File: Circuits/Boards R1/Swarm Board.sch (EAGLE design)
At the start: 90 parts, among them CON1 ISP(2X3), T1 NPN2N2222, T10 TEFT4300, T13 NPN2N2222, T14 NPN2N2222, T15 NPN2N2222, T16 NPN2N2222, T17 NPN2N2222, T18 NPN2N2222, T2 NPN2N2222, T3 NPN2N2222, T4 TEFT4300, T5 TEFT4300, T6 TEFT4300, T7 TEFT4300, T8 TEFT4300, T9 TEFT4300, U1 ATMEGA324P, U3 TB6552FN/FNG

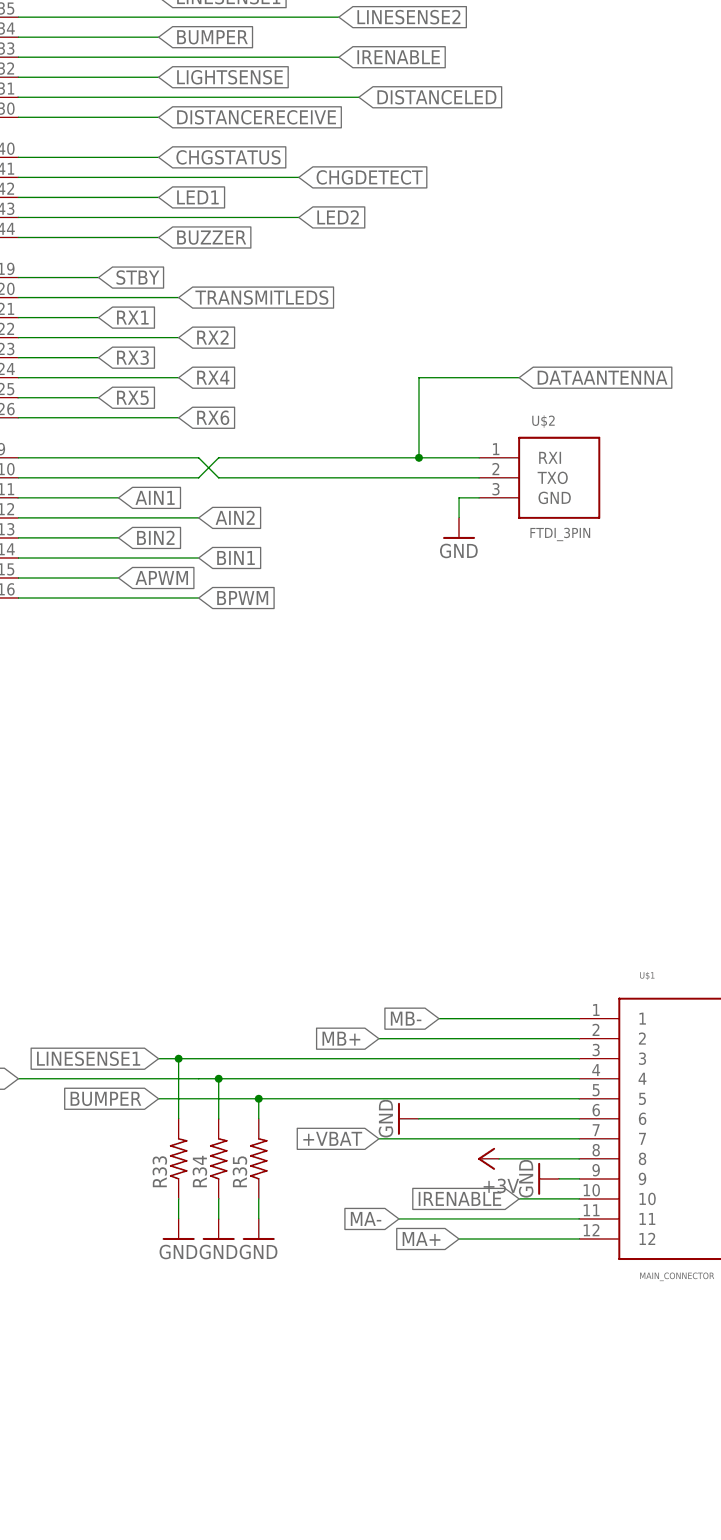
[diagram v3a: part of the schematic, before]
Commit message: 
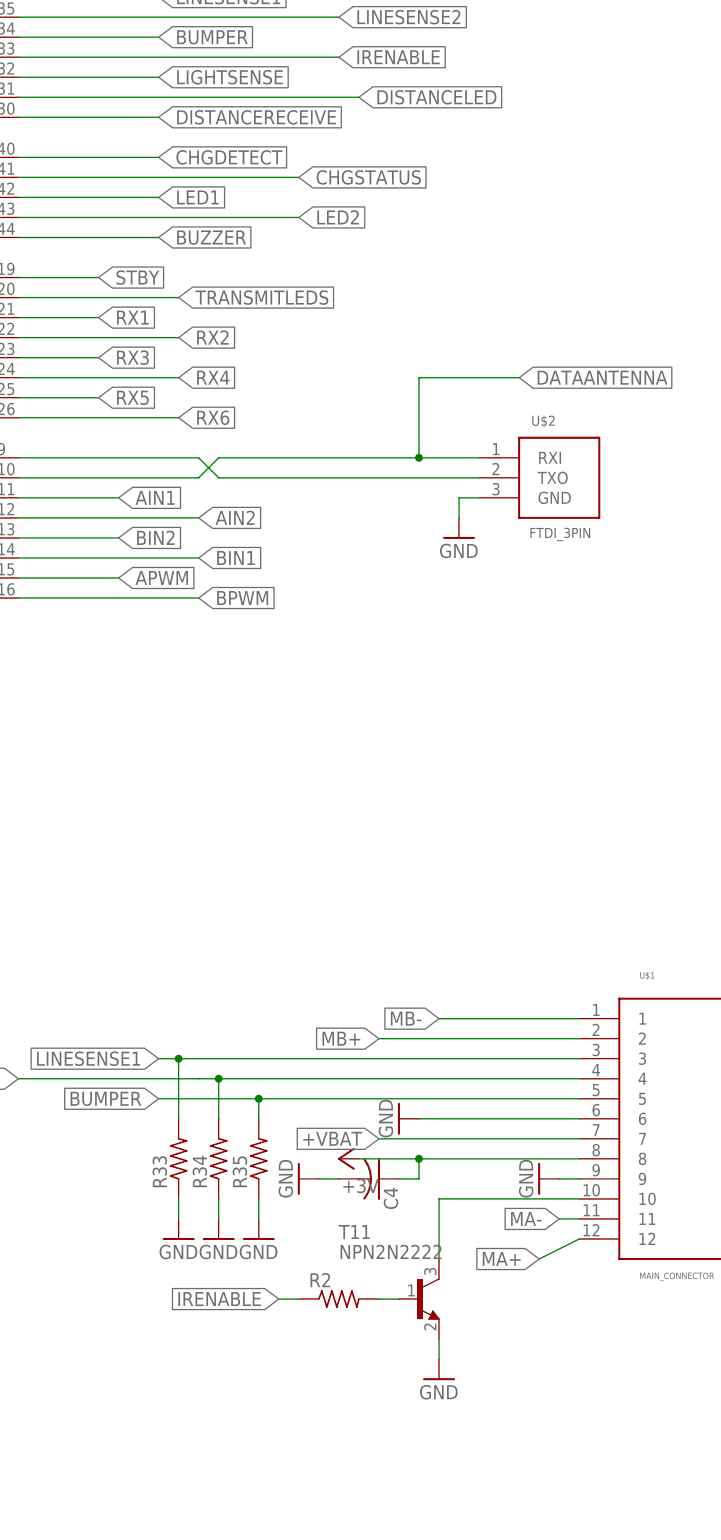
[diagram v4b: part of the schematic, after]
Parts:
- added C4: (no value), Passive:CAP0603
- added R2: (no value), Passive:RES0603
- added T11: NPN2N2222, Passive:NPN2N2222
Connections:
- new net N$4: R2.2, T11.B
- new net N$7: T11.C, U$1.10
- net +3V: now also C4.1
- net CHGDETECT: now also U1.PB0(XCK0/T0/PCINT8); no longer U1.PB1(T1/CLKO/PCINT9)
- net CHGSTATUS: now also U1.PB1(T1/CLKO/PCINT9); no longer U1.PB0(XCK0/T0/PCINT8)
- net GND: now also C4.2, T11.E
- net IRENABLE: now also R2.1; no longer U$1.10
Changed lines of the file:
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@@
 <part name="LED1" library="Passive" deviceset="LED" device="0603" value="red"/>
 <part name="R1" library="Passive" deviceset="RES" device="0603"/>
+<part name="C4" library="Passive" deviceset="CAP" device="0603"/>
+<part name="GND3" library="Supply" deviceset="GND" device=""/>
+<part name="T11" library="Passive" deviceset="NPN2N2222" device=""/>
+<part name="R2" library="Passive" deviceset="RES" device="0603"/>
+<part name="GND26" library="Supply" deviceset="GND" device=""/>
 </parts>
 <sheets>
@@
 <instance part="GND21" gate="1" x="-165.1" y="-48.26"/>
 <instance part="GND20" gate="1" x="96.52" y="-114.3" rot="R270"/>
-<instance part="P+3" gate="1" x="88.9" y="-111.76" rot="R90"/>
+<instance part="P+3" gate="1" x="71.12" y="-111.76" rot="R90"/>
 <instance part="U$3" gate="G$1" x="-114.3" y="93.98"/>
 <instance part="R29" gate="G$1" x="-66.04" y="93.98" rot="R90"/>
@@
 <instance part="LED1" gate="G$1" x="-139.7" y="114.3"/>
 <instance part="R1" gate="G$1" x="-139.7" y="101.6" rot="R90"/>
+<instance part="C4" gate="G$1" x="73.66" y="-114.3" rot="R270"/>
+<instance part="GND3" gate="1" x="66.04" y="-114.3" rot="R270"/>
+<instance part="T11" gate="G$1" x="81.28" y="-129.54"/>
+<instance part="R2" gate="G$1" x="71.12" y="-129.54"/>
+<instance part="GND26" gate="1" x="83.82" y="-139.7"/>
 </instances>
 <busses>
@@
 <segment>
 <pinref part="U$1" gate="G$1" pin="8"/>
-<wire x1="101.6" y1="-111.76" x2="91.44" y2="-111.76" width="0.1524" layer="91"/>
+<wire x1="101.6" y1="-111.76" x2="81.28" y2="-111.76" width="0.1524" layer="91"/>
 <pinref part="P+3" gate="1" pin="+3V"/>
+<pinref part="C4" gate="G$1" pin="1"/>
+<wire x1="81.28" y1="-111.76" x2="73.66" y2="-111.76" width="0.1524" layer="91"/>
+<wire x1="78.74" y1="-114.3" x2="81.28" y2="-114.3" width="0.1524" layer="91"/>
+<wire x1="81.28" y1="-114.3" x2="81.28" y2="-111.76" width="0.1524" layer="91"/>
+<junction x="81.28" y="-111.76"/>
 </segment>
 </net>
@@
 <junction x="-66.04" y="78.74"/>
 </segment>
+<segment>
+<pinref part="C4" gate="G$1" pin="2"/>
+<pinref part="GND3" gate="1" pin="GND"/>
+<wire x1="68.58" y1="-114.3" x2="71.12" y2="-114.3" width="0.1524" layer="91"/>
+</segment>
+<segment>
+<pinref part="T11" gate="G$1" pin="E"/>
+<pinref part="GND26" gate="1" pin="GND"/>
+<wire x1="83.82" y1="-137.16" x2="83.82" y2="-134.62" width="0.1524" layer="91"/>
+</segment>
 </net>
 <net name="+VBAT" class="0">
@@
 <net name="CHGDETECT" class="0">
 <segment>
-<pinref part="U1" gate="G$1" pin="PB1(T1/CLKO/PCINT9)"/>
-<wire x1="30.48" y1="12.7" x2="66.04" y2="12.7" width="0.1524" layer="91"/>
-<label x="66.04" y="12.7" size="1.778" layer="91" xref="yes"/>
-</segment>
-<segment>
 <pinref part="U$3" gate="G$1" pin="!PG"/>
 <wire x1="-124.46" y1="86.36" x2="-139.7" y2="86.36" width="0.1524" layer="91"/>
 <label x="-139.7" y="86.36" size="1.778" layer="91" rot="R180" xref="yes"/>
+</segment>
+<segment>
+<pinref part="U1" gate="G$1" pin="PB0(XCK0/T0/PCINT8)"/>
+<wire x1="30.48" y1="15.24" x2="48.26" y2="15.24" width="0.1524" layer="91"/>
+<label x="48.26" y="15.24" size="1.778" layer="91" xref="yes"/>
 </segment>
 </net>
@@
 <segment>
 <pinref part="U$1" gate="G$1" pin="12"/>
-<wire x1="101.6" y1="-121.92" x2="86.36" y2="-121.92" width="0.1524" layer="91"/>
-<label x="86.36" y="-121.92" size="1.778" layer="91" rot="R180" xref="yes"/>
+<wire x1="101.6" y1="-121.92" x2="96.52" y2="-124.46" width="0.1524" layer="91"/>
+<label x="96.52" y="-124.46" size="1.778" layer="91" rot="R180" xref="yes"/>
 </segment>
 </net>
@@
 <segment>
 <pinref part="U$1" gate="G$1" pin="11"/>
-<wire x1="101.6" y1="-119.38" x2="78.74" y2="-119.38" width="0.1524" layer="91"/>
-<label x="78.74" y="-119.38" size="1.778" layer="91" rot="R180" xref="yes"/>
+<wire x1="101.6" y1="-119.38" x2="99.06" y2="-119.38" width="0.1524" layer="91"/>
+<label x="99.06" y="-119.38" size="1.778" layer="91" rot="R180" xref="yes"/>
 </segment>
 </net>
@@
 <net name="CHGSTATUS" class="0">
 <segment>
-<pinref part="U1" gate="G$1" pin="PB0(XCK0/T0/PCINT8)"/>
-<wire x1="30.48" y1="15.24" x2="48.26" y2="15.24" width="0.1524" layer="91"/>
-<label x="48.26" y="15.24" size="1.778" layer="91" xref="yes"/>
-</segment>
-<segment>
 <pinref part="U$3" gate="G$1" pin="STAT2"/>
 <wire x1="-124.46" y1="91.44" x2="-139.7" y2="91.44" width="0.1524" layer="91"/>
 <label x="-139.7" y="91.44" size="1.778" layer="91" rot="R180" xref="yes"/>
+</segment>
+<segment>
+<pinref part="U1" gate="G$1" pin="PB1(T1/CLKO/PCINT9)"/>
+<wire x1="30.48" y1="12.7" x2="66.04" y2="12.7" width="0.1524" layer="91"/>
+<label x="66.04" y="12.7" size="1.778" layer="91" xref="yes"/>
 </segment>
 </net>
@@
 </segment>
 <segment>
-<pinref part="U$1" gate="G$1" pin="10"/>
-<wire x1="101.6" y1="-116.84" x2="93.98" y2="-116.84" width="0.1524" layer="91"/>
-<label x="93.98" y="-116.84" size="1.778" layer="91" rot="R180" xref="yes"/>
+<pinref part="R2" gate="G$1" pin="1"/>
+<wire x1="66.04" y1="-129.54" x2="63.5" y2="-129.54" width="0.1524" layer="91"/>
+<label x="63.5" y="-129.54" size="1.778" layer="91" rot="R180" xref="yes"/>
 </segment>
 </net>
@@
 </segment>
 </net>
+<net name="N$4" class="0">
+<segment>
+<pinref part="T11" gate="G$1" pin="B"/>
+<pinref part="R2" gate="G$1" pin="2"/>
+<wire x1="76.2" y1="-129.54" x2="78.74" y2="-129.54" width="0.1524" layer="91"/>
+</segment>
+</net>
+<net name="N$7" class="0">
+<segment>
+<pinref part="U$1" gate="G$1" pin="10"/>
+<wire x1="101.6" y1="-116.84" x2="83.82" y2="-116.84" width="0.1524" layer="91"/>
+<wire x1="83.82" y1="-116.84" x2="83.82" y2="-124.46" width="0.1524" layer="91"/>
+<pinref part="T11" gate="G$1" pin="C"/>
+</segment>
+</net>

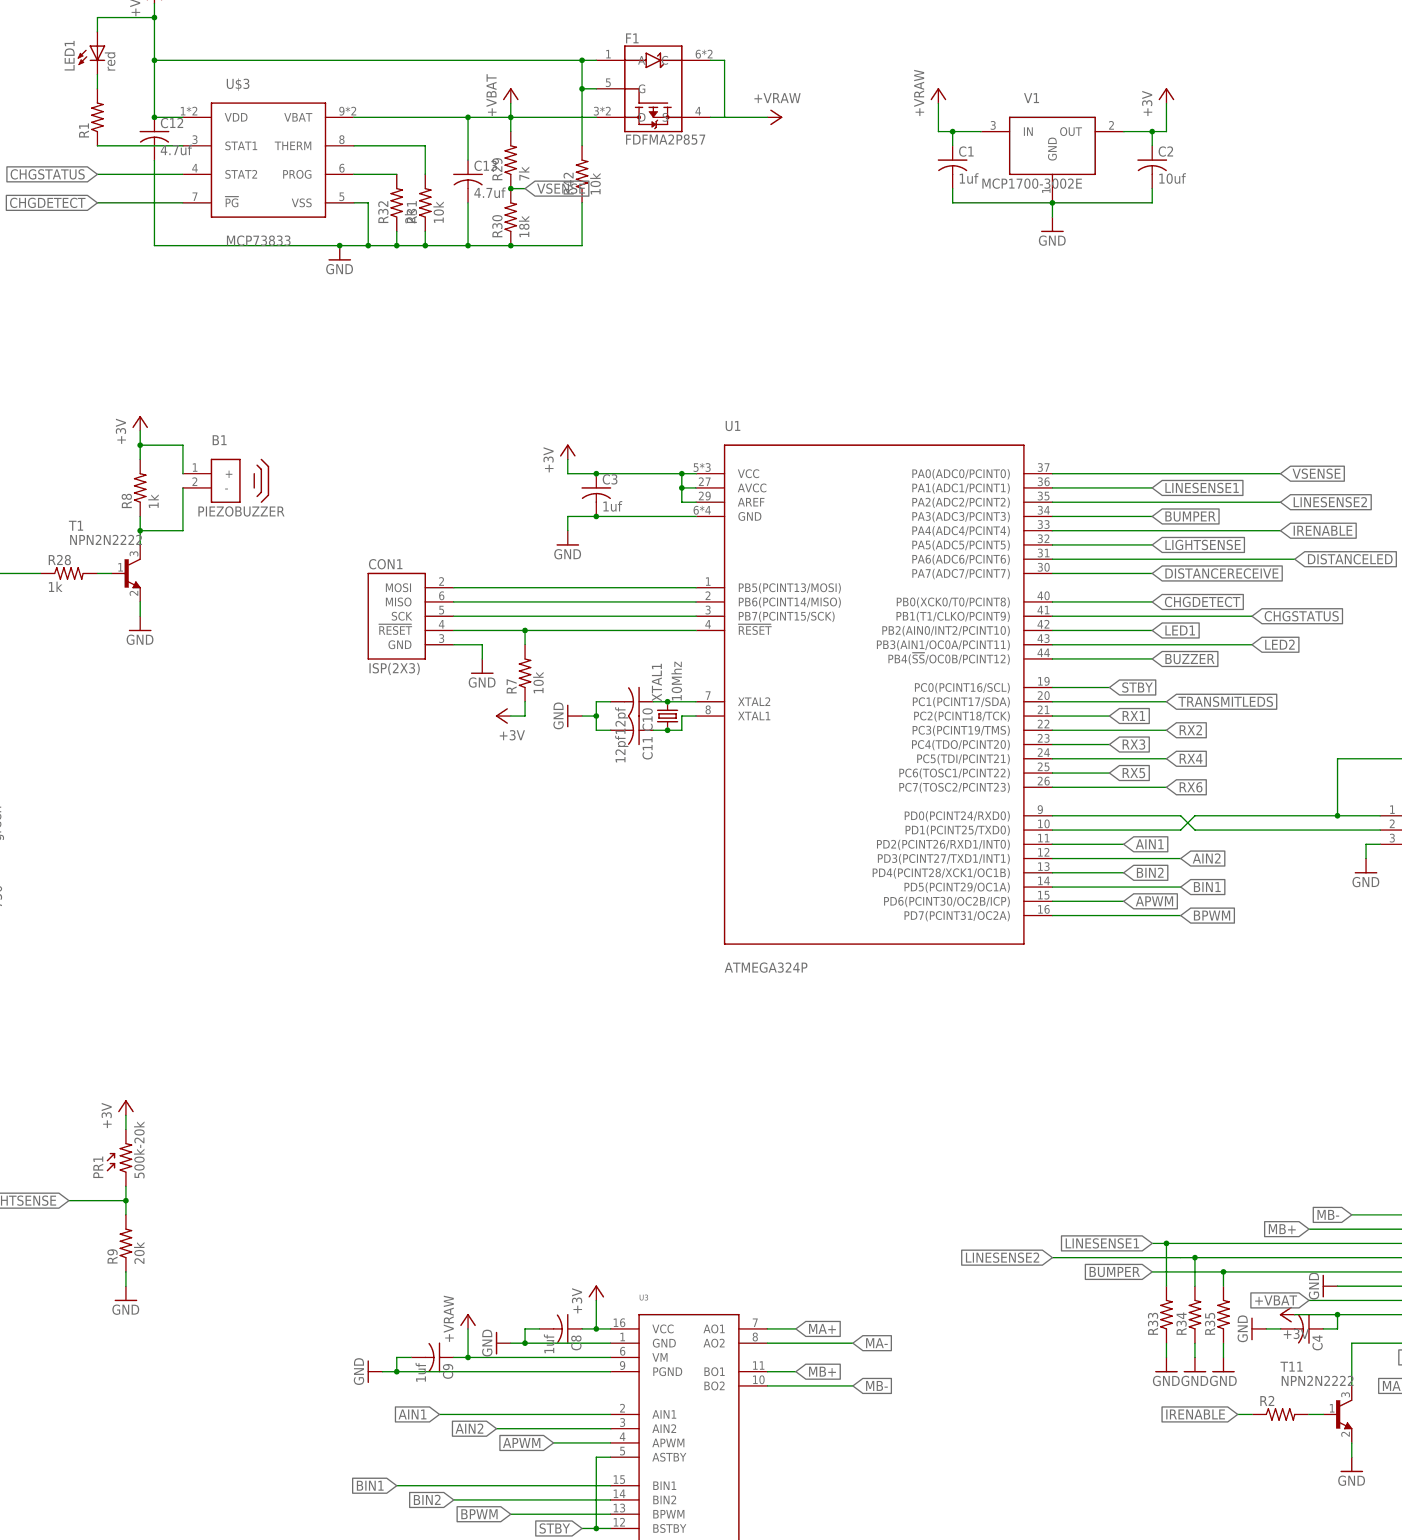
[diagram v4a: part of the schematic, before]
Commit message: 
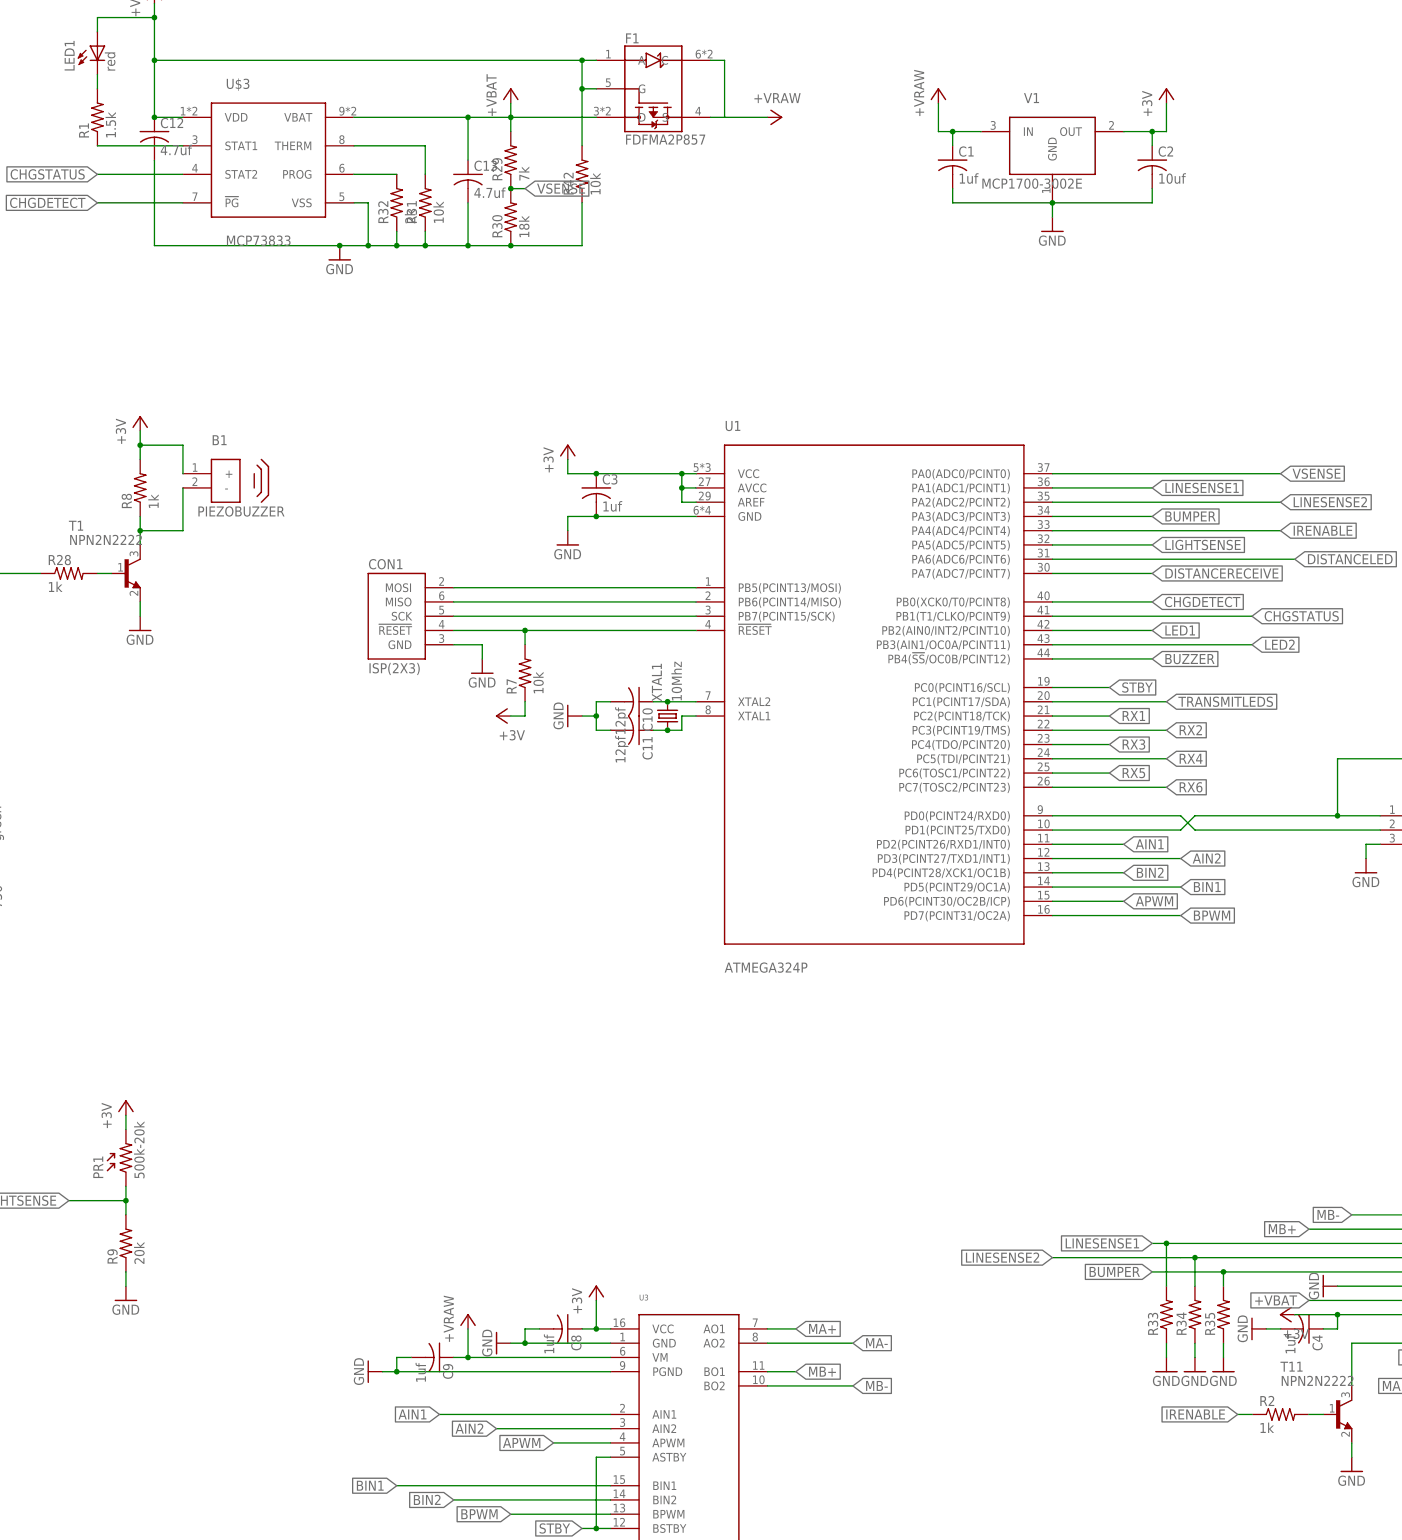
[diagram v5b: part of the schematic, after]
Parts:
- C4: value (none) -> 1uf
- R1: value (none) -> 1.5k
- R2: value (none) -> 1k
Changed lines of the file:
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@@
 <part name="P+13" library="Supply" deviceset="+VRAW" device=""/>
 <part name="LED1" library="Passive" deviceset="LED" device="0603" value="red"/>
-<part name="R1" library="Passive" deviceset="RES" device="0603"/>
-<part name="C4" library="Passive" deviceset="CAP" device="0603"/>
+<part name="R1" library="Passive" deviceset="RES" device="0603" value="1.5k"/>
+<part name="C4" library="Passive" deviceset="CAP" device="0603" value="1uf"/>
 <part name="GND3" library="Supply" deviceset="GND" device=""/>
 <part name="T11" library="Passive" deviceset="NPN2N2222" device=""/>
-<part name="R2" library="Passive" deviceset="RES" device="0603"/>
+<part name="R2" library="Passive" deviceset="RES" device="0603" value="1k"/>
 <part name="GND26" library="Supply" deviceset="GND" device=""/>
 </parts>
